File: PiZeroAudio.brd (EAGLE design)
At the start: 65.1 x 30.2 mm, 55 parts, among them CN1 1X4-BIG, CON1 RPI-ZERO, J1 1X2-3.5MM, U1 TXB0104PWR, U2 LSM6DS33, U3 NC7WZ16, U4 TPA3144D2PWPR

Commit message: Added LED
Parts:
- added D1: (no value), diode:SMB
- added JP2: (no value), adafruit:1X03
- added LED1: (no value), adafruit:CHIP-LED0805
- added R16, R17: 220, adafruit:R0603
- moved SH1 2.56 mm to (-33.5, 22.0)
- moved C1 1.14 mm to (-33.5, 22.8), turned to 90 degrees
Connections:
- new net N$6: LED1.C, R16.2
- new net PWR-IN: D1.A, J1.2
- new net PWR-LED: JP2.2, R17.1
- net +3V3: now also JP2.1, LED1.A, R17.2
- net +5V: now also D1.C; no longer J1.2
- net GND: now also JP2.3, R16.1
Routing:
- net GND: track 21.2 -> 30.9 mm
- net AN3V3: track 0.00 -> 7.40 mm, vias 0 -> 2
- net AGND: track 78.1 -> 85.0 mm
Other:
- board text added: "+3"
- board text added: "0"
- board text added: "LED"

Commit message: Pre- grove connector
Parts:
- removed CN1: 1X4-BIG, adafruit:1X04-BIG
- removed D1: (no value), diode:SMB
- added J2: 4X1-LOCKING, HappyBrackets:22-23-2041
- added Q1: DMG2305UX, HappyBrackets:SOT23
- added R18: 33K, adafruit:R0603
- added R19: 10R, adafruit:R0603
- added U5: TPA3144D2PWPR, HappyBrackets:HTSSOP28
- J1: value 1X2-3.5MM -> 2X1-LOCKING; device adafruit:1X2-3.5MM -> HappyBrackets:22-23-2021
- JP1: value GPIO -> (none); device adafruit:2X04 -> adafruit:1X03
- JP2: value (none) -> GPIO; device adafruit:1X03 -> adafruit:2X04
- R1, R2: value 10K -> 220
- R10: value 39K -> 1K8
- R11: value 56K -> 10K
- R12: value 33K -> 47K
- R13: value 33K -> 10K
- R14: value 33K -> 39K
- R15: value 10R -> 56K
- R16, R17: value 220 -> 33K
- R3: value 220 -> 10K
- R4: value 100 -> 10K
- R5, R8: value 1K8 -> 220
- R6: value 220 -> 100
- R7: value 100 -> 1K8
- R9: value 10K -> 100
- U4: value TPA3144D2PWPR -> DMMT5401; device HappyBrackets:HTSSOP28 -> HappyBrackets:SOT26-TRANS
- moved R1 53.5 mm to (-15.8, 9.96), turned to 270 degrees
- moved R3 44.2 mm to (-67.5, 23.3), turned to 90 degrees
- moved R2 43.1 mm to (-18.9, 9.91), turned to 270 degrees
- moved R4 37.3 mm to (-60.0, 22.9), turned to 90 degrees
- moved R9 20.5 mm to (-33.1, 19.1), turned to 180 degrees
- moved R11 18.8 mm to (-53.3, 22.9), turned to 270 degrees
- moved R17 17.9 mm to (-33.1, 5.46), turned to 180 degrees
- moved R13 17.0 mm to (-50.0, 3.68), turned to 90 degrees
- moved R6 16.4 mm to (-24.1, 12.7)
- moved JP1 16.3 mm to (-24.7, 3.71), turned to 180 degrees
- moved JP2 16.3 mm to (-17.1, 18.2), turned to 270 degrees
- moved R16 14.4 mm to (-33.1, 7.62), turned to 0 degrees
- moved R12 13.3 mm to (-46.4, 6.20), turned to 180 degrees
- moved R15 12.4 mm to (-39.3, 11.5), turned to 0 degrees
- moved R5 10.8 mm to (-24.1, 15.0), turned to 0 degrees
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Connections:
- removed net PWR-IN: D1.A, J1.2
- new net +5V-IN: J1.1, Q1.S, U4.E1
- new net N$22: R13.1, U4.B1, U4.B2, U4.C2
- new net N$27: Q1.G, R12.1, U4.C1
- net +3V3: now also JP1.1, R1.2, R3.1, R4.1; no longer JP2.1, R1.1, R17.2, R2.1
- net +5V: now also Q1.D, R19.2, U4.E2, U5.15, U5.16, U5.27, U5.28; no longer D1.C, R15.2, U4.15, U4.16, U4.27, U4.28
- net /MUTE: now also R11.1; no longer R9.1
- net AGND: now also J1.2, R10.1, R13.2, R14.2, R16.2, R6.1, R9.1, U5.10, U5.13, U5.19, U5.24, U5.GND@10, U5.GND@11, U5.GND@12, U5.GND@13, U5.GND@14, U5.GND@15, U5.GND@16, U5.GND@17, U5.GND@18, U5.GND@19, U5.GND@20, U5.GND@21, U5.GND@22, U5.GND@23, U5.GND@24, U5.GND@25, U5.GND@26, U5.GND@27, U5.GND@28, U5.GND@29, U5.GND@30, U5.GND@PAD; no longer J1.1, R10.2, R4.1, R5.1, R8.1, U4.10, U4.13, U4.19, U4.24, U4.GND@10, U4.GND@11, U4.GND@12, U4.GND@13, U4.GND@14, U4.GND@15, U4.GND@16, U4.GND@17, U4.GND@18, U4.GND@19, U4.GND@20, U4.GND@21, U4.GND@22, U4.GND@23, U4.GND@24, U4.GND@25, U4.GND@26, U4.GND@27, U4.GND@28, U4.GND@29, U4.GND@30, U4.GND@PAD
- net AUDIO-LEFT: now also R7.2, U5.3; no longer R5.2, U4.3
- net AUDIO-RIGHT: now also R10.2, U5.12; no longer R8.2, U4.12
- net GND: now also JP1.3, JP2.2, JP2.4, JP2.6, JP2.8, R2.1; no longer JP1.2, JP1.4, JP1.6, JP1.8, JP2.3, R16.1
- net L+: now also J2.4; no longer CN1.1
- net L-: now also J2.3; no longer CN1.2
- net N$1: now also R5.1, R6.2; no longer R3.1, R4.2
- net N$10: now also U5.17; no longer U4.17
- net N$11: now also JP2.1; no longer JP1.1
- net N$12: now also JP2.3; no longer JP1.3
- net N$13: now also U5.21; no longer U4.21
- net N$14: now also JP2.5; no longer JP1.5
- net N$15: now also JP2.7; no longer JP1.7
- net N$16: now also U5.22; no longer U4.22
- net N$17: now also U5.26; no longer U4.26
- net N$18: now also U5.25; no longer U4.25
- net N$19: now also U5.23; no longer U4.23
- net N$2: now also R5.2; no longer R3.2
- net N$20: now also U5.20; no longer U4.20
- net N$21: now also U5.18; no longer U4.18
- net N$23: now also R16.1, R17.2, U5.6; no longer R12.1, R13.2, U4.6
- net N$24: now also R17.1, R18.2, U5.7; no longer R13.1, R14.2, U4.7
- net N$25: now also R14.1, R15.2, U5.8; no longer R10.1, R11.2, U4.8
- net N$26: now also R15.1, R18.1, U5.5, U5.9; no longer R11.1, R14.1, U4.5, U4.9
- net N$3: now also R8.2; no longer R6.2
- net N$4: now also R8.1, R9.2; no longer R6.1, R7.2
- net N$5: now also R11.2, U5.1, U5.2; no longer R9.2, U4.1, U4.2
- net N$6: now also R2.2; no longer R16.2
- net N$7: now also U5.4; no longer U4.4
- net N$8: now also U5.11; no longer U4.11
- net N$9: now also R19.1, U5.14; no longer R15.1, U4.14
- net PWR-LED: now also JP1.2, R1.1; no longer JP2.2, R17.1
- net R+: now also J2.1; no longer CN1.4
- net R-: now also J2.2; no longer CN1.3
- net SCL: now also R4.2; no longer R2.2
- net SDA: now also R3.2; no longer R1.2
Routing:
- net +5V-IN: track 0.00 -> 6.41 mm
- net N$22: track 0.00 -> 5.23 mm
- net N$27: track 0.00 -> 5.10 mm
- net AGND: track 85.0 -> 86.9 mm
- net R+: track 13.7 -> 12.3 mm
- net L+: track 14.7 -> 13.9 mm
- net L-: track 13.6 -> 13.0 mm
- net N$26: track 28.5 -> 27.9 mm
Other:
- board text added: "+5"
- board text added: "L+"
- board text added: "L-"
- board text added: "R+"
- board text added: "R-"
- board text removed: "+3"
- board text removed: "LED"

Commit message: PostGrove
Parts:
- removed JP2: GPIO, adafruit:2X04
- added J3: GROVE, HappyBrackets:JST-PH4
- added J4: 2X2HEADER, HappyBrackets:2X2
- moved R2 12.1 mm to (-30.1, 5.05), turned to 90 degrees
- moved R1 8.20 mm to (-23.8, 8.15), turned to 180 degrees
- moved LED1 4.04 mm to (-27.2, 7.92)
- moved JP1 0.91 mm to (-24.5, 2.82)
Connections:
- removed net N$11: JP2.1, U1.13
- removed net N$12: JP2.3, U1.12
- removed net N$14: JP2.5, U1.11
- removed net N$15: JP2.7, U1.10
- new net GPI022-OUT: J4.1, U1.11
- new net GPIO21-OUT: J4.3, U1.10
- new net GPIO23-OUT: J3.1, U1.12
- new net GPIO25-OUT: J3.2, U1.13
- net +5V: now also J3.3
- net GND: now also J3.4, J4.2, J4.4; no longer JP2.2, JP2.4, JP2.6, JP2.8
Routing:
- net GPIO21-OUT: track 0.00 -> 13.6 mm
- net GPI022-OUT: track 0.00 -> 11.9 mm
- net N$15: track 9.10 -> 0.00 mm
- net GPIO23-OUT: track 0.00 -> 9.04 mm
- net GPIO25-OUT: track 0.00 -> 7.61 mm
- net N$14: track 7.36 -> 0.00 mm
- net N$12: track 5.45 -> 0.00 mm
- net N$11: track 3.75 -> 0.00 mm

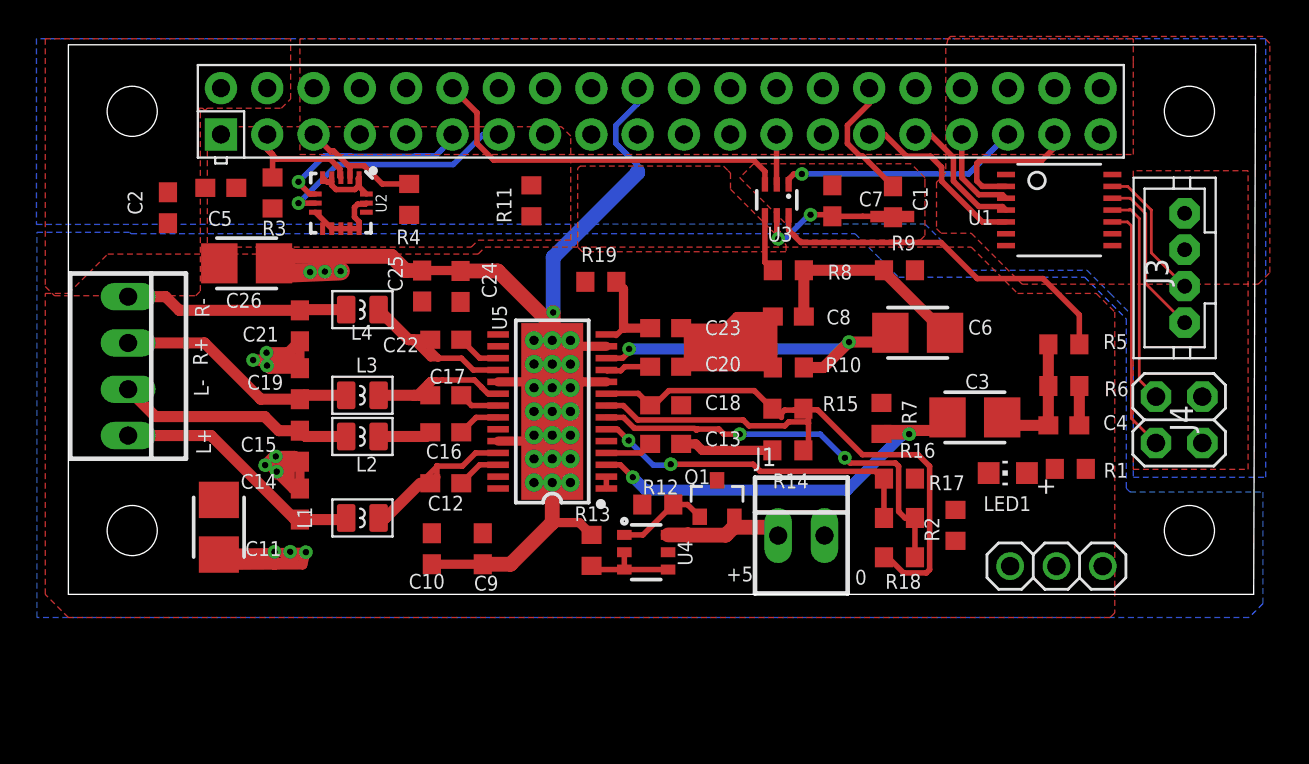
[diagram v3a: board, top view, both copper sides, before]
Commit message: Rout complete and rats nest. Need to complete pour
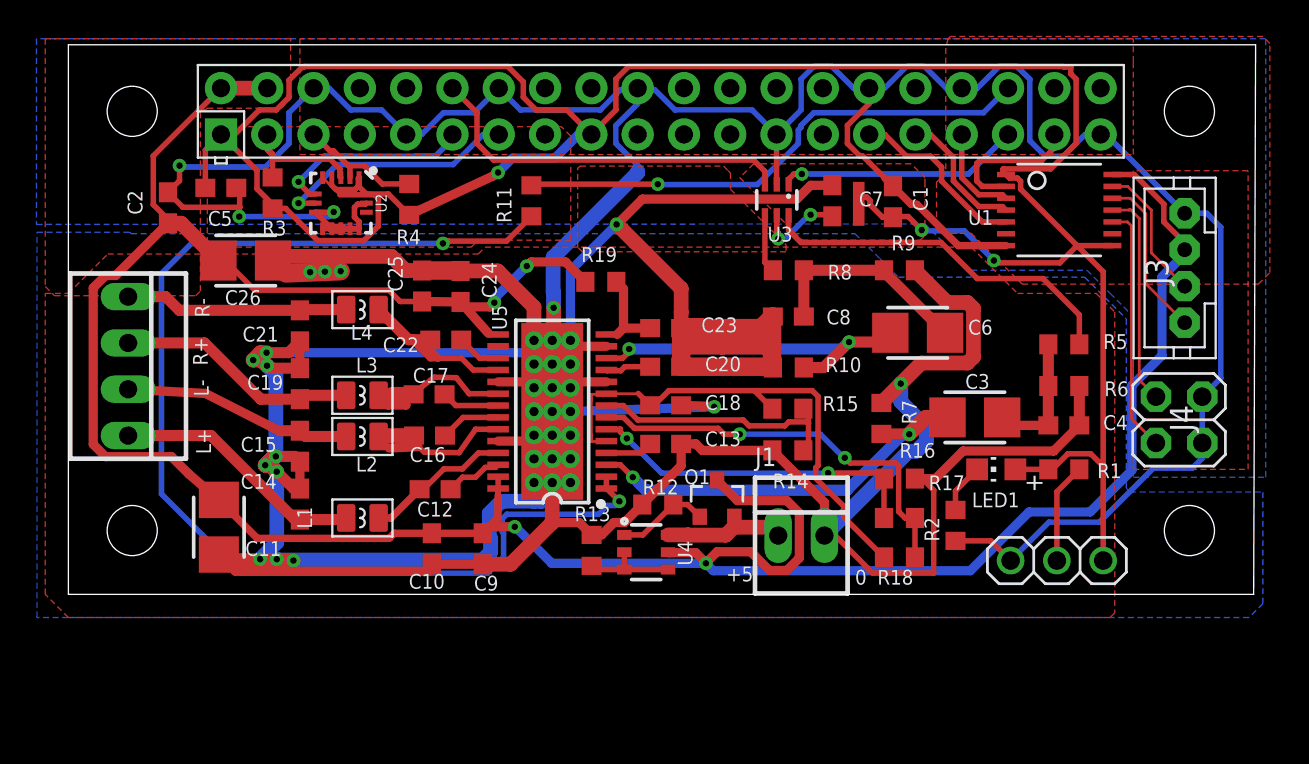
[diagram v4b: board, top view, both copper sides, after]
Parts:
- moved SH1 2.05 mm to (-35.4, 22.8), turned to 90 degrees
- moved C17 0.92 mm to (-59.0, 12.2)
- moved C16 0.91 mm to (-58.9, 9.98)
- moved C12 0.67 mm to (-58.6, 7.04)
- moved LED1 0.67 mm to (-27.8, 8.13)
- moved R1 0.36 mm to (-24.1, 8.13)
- moved JP1 0.31 mm to (-24.5, 3.12)
- moved C26 0.16 mm to (-69.0, 19.6)
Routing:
- net AGND: track 86.9 -> 322.2 mm, vias 12 -> 15
- net +5V: track 0.00 -> 156.8 mm, vias 0 -> 4
- net +3V3: track 4.19 -> 146.2 mm, vias 0 -> 3
- net GND: track 30.9 -> 159.2 mm, vias 1 -> 4
- net N$5: track 0.65 -> 65.3 mm, vias 0 -> 2
- net /MUTE: track 0.00 -> 28.9 mm, vias 0 -> 1
- net N$19: track 2.93 -> 10.5 mm
- net PWR-LED: track 0.00 -> 5.51 mm
- net N$6: track 0.00 -> 2.71 mm
- net AN3V3: track 7.40 -> 4.87 mm
- net N$16: track 2.36 -> 3.32 mm
- net N$13: track 2.26 -> 3.19 mm
- net N$1: track 6.38 -> 7.16 mm
- net N$17: track 2.44 -> 3.16 mm
- net N$18: track 8.72 -> 8.03 mm
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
